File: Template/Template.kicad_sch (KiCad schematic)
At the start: 19 parts

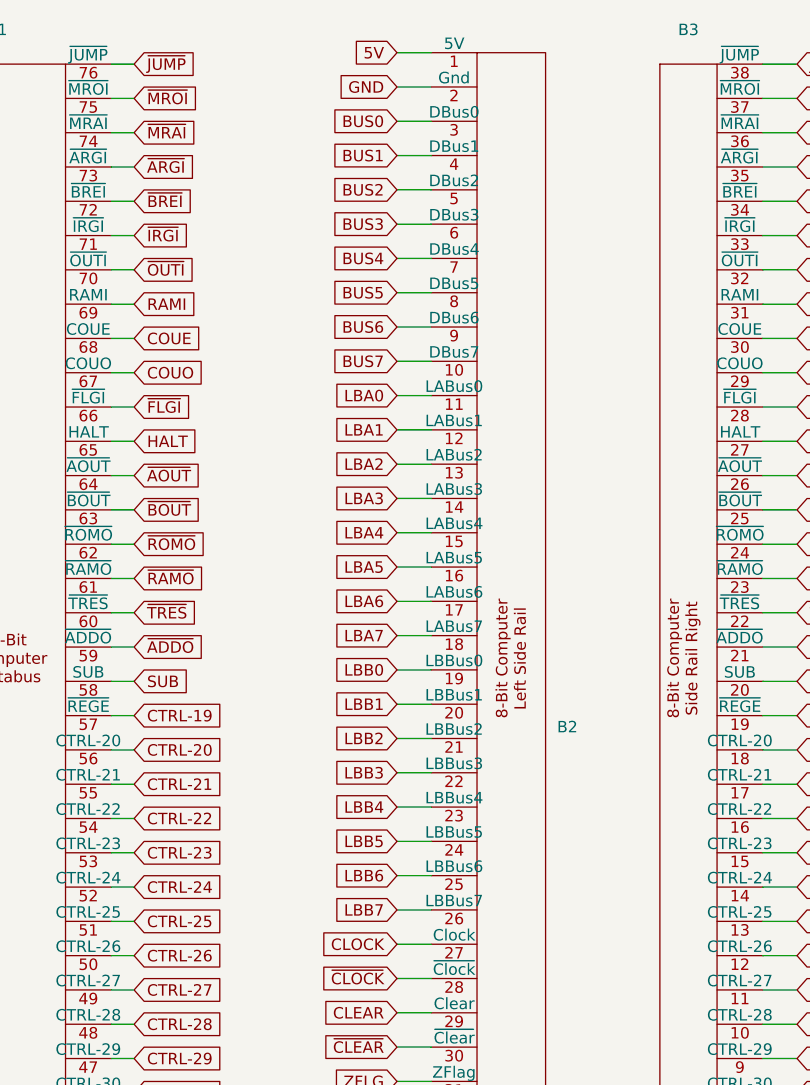
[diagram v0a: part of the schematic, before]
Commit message: Fixed some issues with the orientation of the local buses on the side-rails.
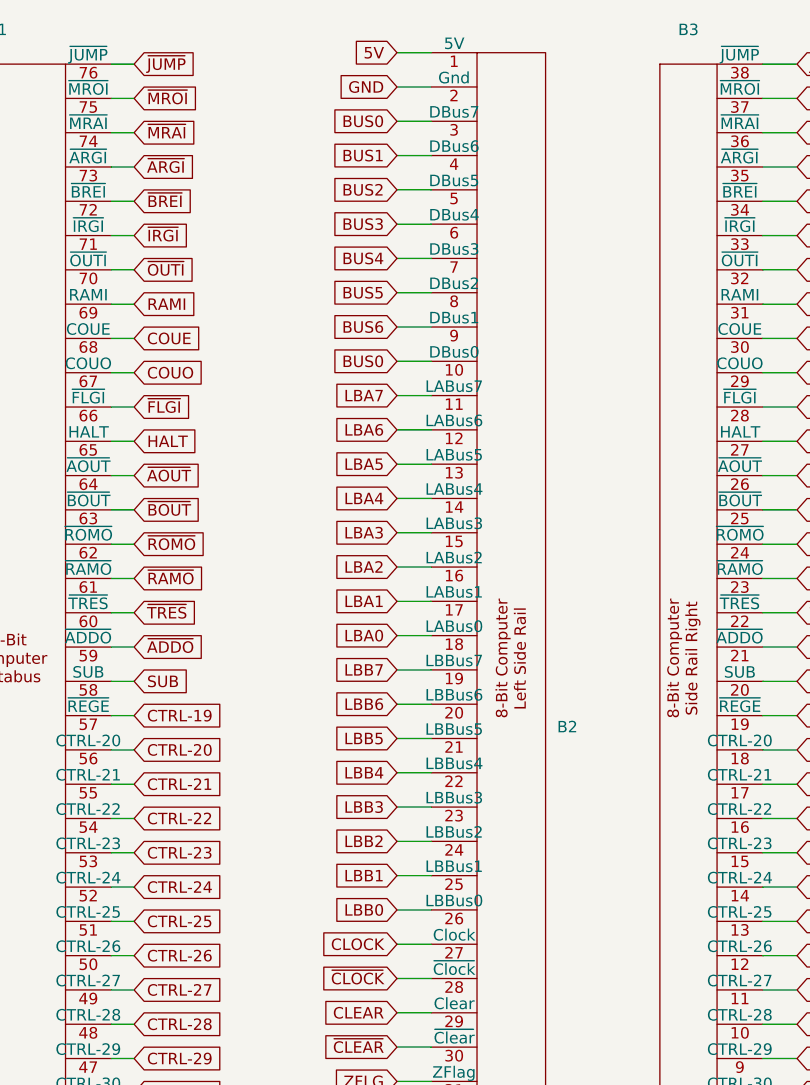
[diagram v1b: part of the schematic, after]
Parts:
- B1, B2, B3: value ~ -> (none)
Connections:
- net BUS0: now also B2.10 (DBus0)
- net BUS7: no longer B2.10 (DBus7)
- net LBA0: now also B2.18 (LABus0); no longer B2.11 (LABus0)
- net LBA1: now also B2.17 (LABus1); no longer B2.12 (LABus1)
- net LBA2: now also B2.16 (LABus2); no longer B2.13 (LABus2)
- net LBA3: now also B2.15 (LABus3); no longer B2.14 (LABus3)
- net LBA4: now also B2.14 (LABus4); no longer B2.15 (LABus4)
- net LBA5: now also B2.13 (LABus5); no longer B2.16 (LABus5)
- net LBA6: now also B2.12 (LABus6); no longer B2.17 (LABus6)
- net LBA7: now also B2.11 (LABus7); no longer B2.18 (LABus7)
- net LBB0: now also B2.26 (LBBus0); no longer B2.19 (LBBus0)
- net LBB1: now also B2.25 (LBBus1); no longer B2.20 (LBBus1)
- net LBB2: now also B2.24 (LBBus2); no longer B2.21 (LBBus2)
- net LBB3: now also B2.23 (LBBus3); no longer B2.22 (LBBus3)
- net LBB4: now also B2.22 (LBBus4); no longer B2.23 (LBBus4)
- net LBB5: now also B2.21 (LBBus5); no longer B2.24 (LBBus5)
- net LBB6: now also B2.20 (LBBus6); no longer B2.25 (LBBus6)
- net LBB7: now also B2.19 (LBBus7); no longer B2.26 (LBBus7)

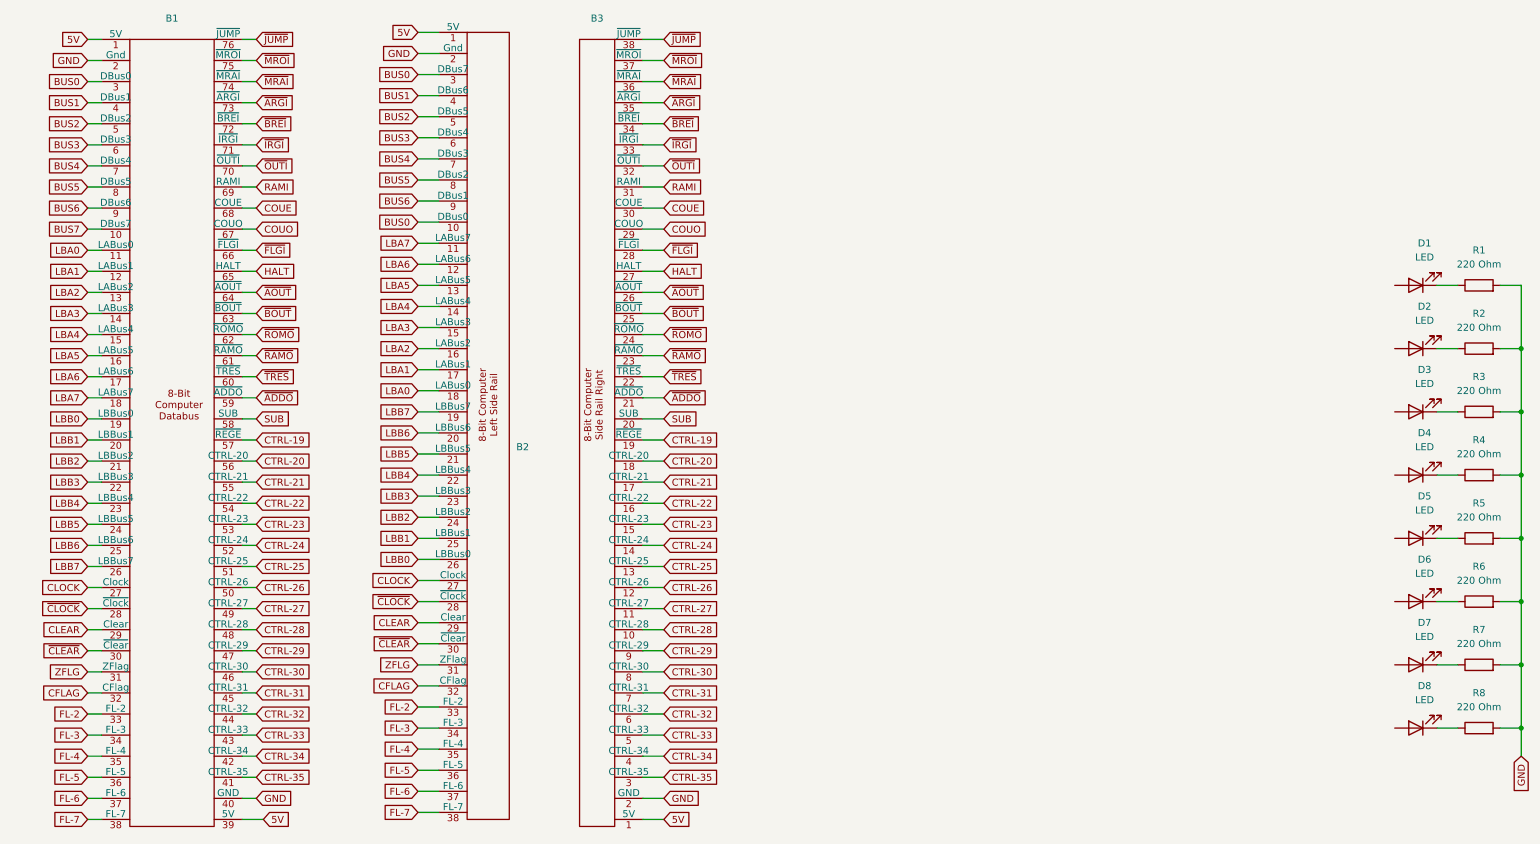
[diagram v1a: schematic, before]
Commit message: [Template] - fixed the ordering of the buses in the schematic and PCB labels. Bit 0 is now always at the top.
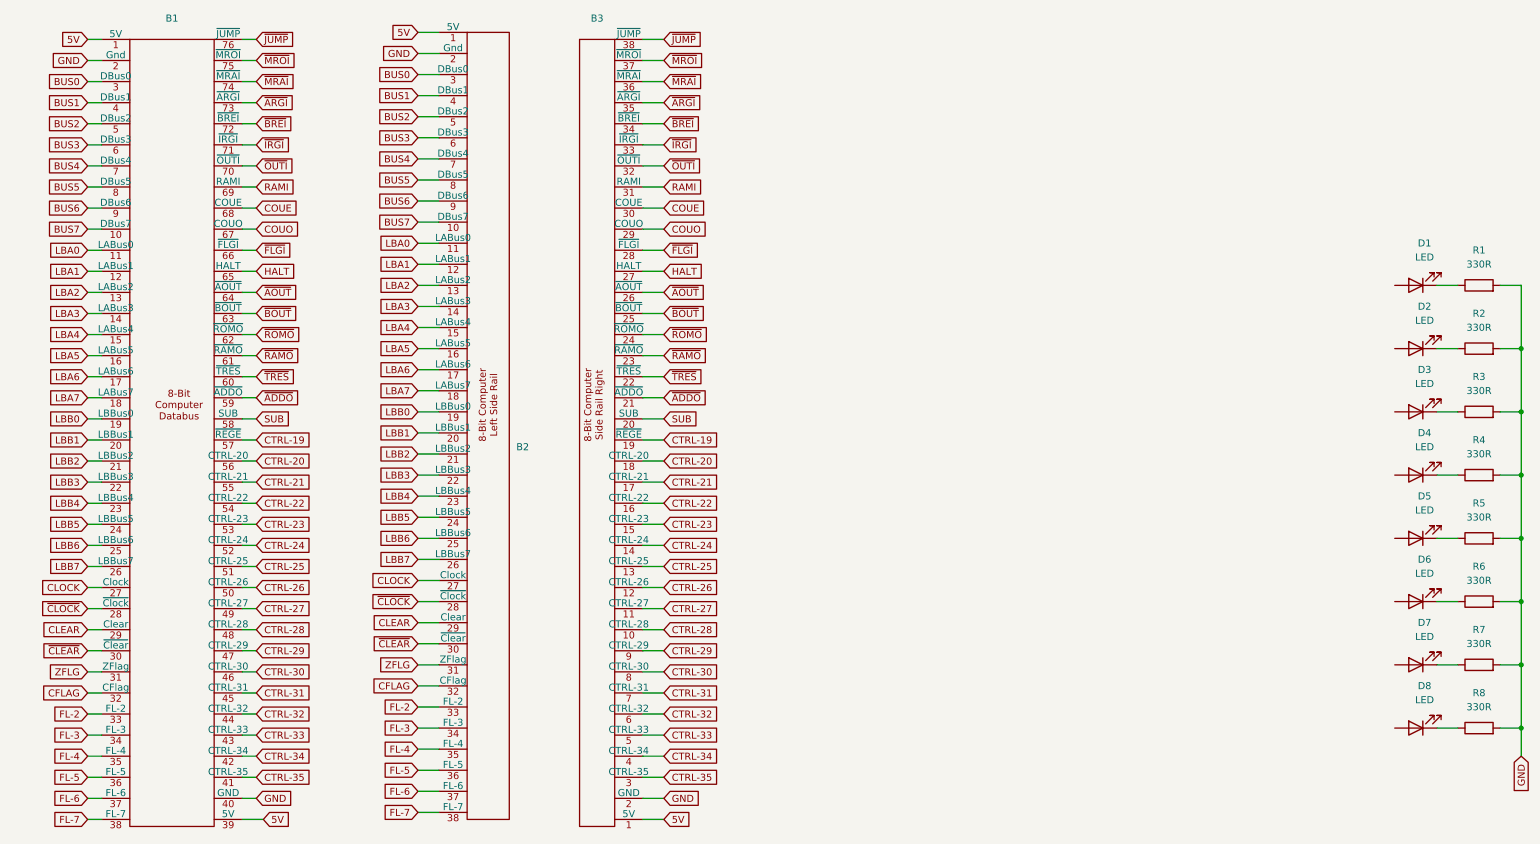
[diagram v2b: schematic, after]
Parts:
- R1, R2, R3, R4, R5, R6, R7, R8: value 220 Ohm -> 330R
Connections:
- net BUS0: no longer B2.10 (DBus0)
- net BUS7: now also B2.10 (DBus7)
- net LBA0: now also B2.11 (LABus0); no longer B2.18 (LABus0)
- net LBA1: now also B2.12 (LABus1); no longer B2.17 (LABus1)
- net LBA2: now also B2.13 (LABus2); no longer B2.16 (LABus2)
- net LBA3: now also B2.14 (LABus3); no longer B2.15 (LABus3)
- net LBA4: now also B2.15 (LABus4); no longer B2.14 (LABus4)
- net LBA5: now also B2.16 (LABus5); no longer B2.13 (LABus5)
- net LBA6: now also B2.17 (LABus6); no longer B2.12 (LABus6)
- net LBA7: now also B2.18 (LABus7); no longer B2.11 (LABus7)
- net LBB0: now also B2.19 (LBBus0); no longer B2.26 (LBBus0)
- net LBB1: now also B2.20 (LBBus1); no longer B2.25 (LBBus1)
- net LBB2: now also B2.21 (LBBus2); no longer B2.24 (LBBus2)
- net LBB3: now also B2.22 (LBBus3); no longer B2.23 (LBBus3)
- net LBB4: now also B2.23 (LBBus4); no longer B2.22 (LBBus4)
- net LBB5: now also B2.24 (LBBus5); no longer B2.21 (LBBus5)
- net LBB6: now also B2.25 (LBBus6); no longer B2.20 (LBBus6)
- net LBB7: now also B2.26 (LBBus7); no longer B2.19 (LBBus7)
